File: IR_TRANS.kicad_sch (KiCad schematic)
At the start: 13 parts, among them Q10 XYC-PT204B-L1, U3 HT2348ARTZ8

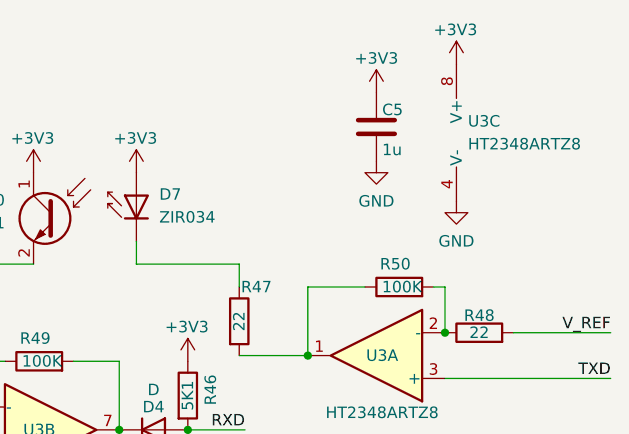
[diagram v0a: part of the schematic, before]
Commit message: update online version before change to esp32 s3
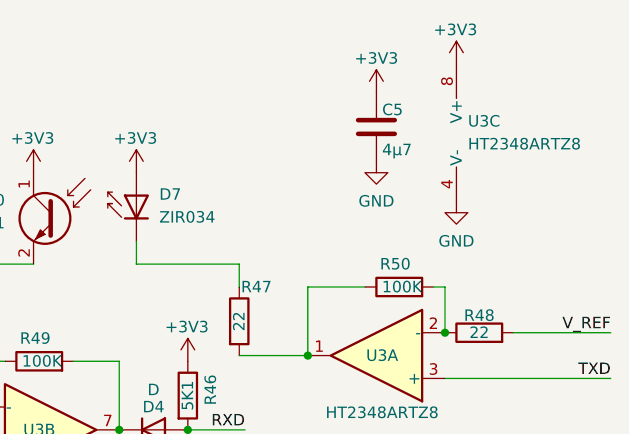
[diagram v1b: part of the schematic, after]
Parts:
- C5: value 1u -> 4µ7; LCSC C5673 -> C69335
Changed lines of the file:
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@@
 			)
 		)
-		(property "Value" "1u"
+		(property "Value" "4µ7"
 			(at 150.495 76.2 0)
 			(effects
@@
 			)
 		)
-		(property "LCSC" "C5673"
+		(property "LCSC" "C69335"
 			(at 149.86 73.66 0)
 			(effects

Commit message: Order V1
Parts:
- removed R32: 22, Resistor_SMD:R_0603_1608Metric, symbol Device:R
- added R14, R15, R24: 1K1, Resistor_SMD:R_0603_1608Metric, symbol Device:R
- D7, Q10: now not fitted; now left out of the parts list
- R21: value 5K1 -> 1K1; LCSC C26000 -> C2906975
- R48: value 22 -> 1K1; LCSC C1203 -> C2906975
- U3: value HT2348ARTZ8 -> LM358LVIDDFR; LCSC C5143016 -> C1849428
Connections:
- net +3V3: now also R15.1
- net TX: now also R48.2; no longer U3.3 (+)
- net VREF: now also U3.2 (-), R24.1; no longer R48.2
- net at R48.1, R50.2: now also U3.3 (+); no longer U3.2 (-)
- net at U3.5 (+): now also R49.1, R24.2
- net at R21.2, R22.2, U3.6 (-): no longer R49.1
- net at Q10.2 (E), R22.1: now also R14.2
- new net: R14.1, R15.2
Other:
- moved on the sheet: C5, D4, R21, R22, R46, R47, R48, R49, R50, U3A, U3B, U3C

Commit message: Upload order version 1.3
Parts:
- removed D7: ZIR034, TheBrutzlers_Lib:SIDE_LED_IR_3mm, symbol theBrutzler:ZIR034
- removed Q10: XYC-PT204B-L1, TheBrutzlers_Lib:SIDE_LED_IR_3mm, symbol Sensor_Optical:BPW40
- added U1: VSMB10940, easyeda2kicad:LED-SMD_3P-L3.0-W1.0-FD, symbol easyeda2kicad:VSMB10940
- added U5: PT12-21B/TR8, easyeda2kicad:LED-SMD_3P-L3.0-W1.0-FD, symbol easyeda2kicad:VSMB10940
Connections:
- net +3V3: now also U1.2, U5.2
- net at R47.1: now also U1.3
- net at R14.2, R22.1: now also U5.3
